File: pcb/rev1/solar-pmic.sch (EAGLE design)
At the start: 82 parts, among them IC2 MCP6002, IC3 MCP6002, IC4 LM3671MF-ADJ, IC5 TS520525, IC6 STM32F030X4, Q1 BSS123

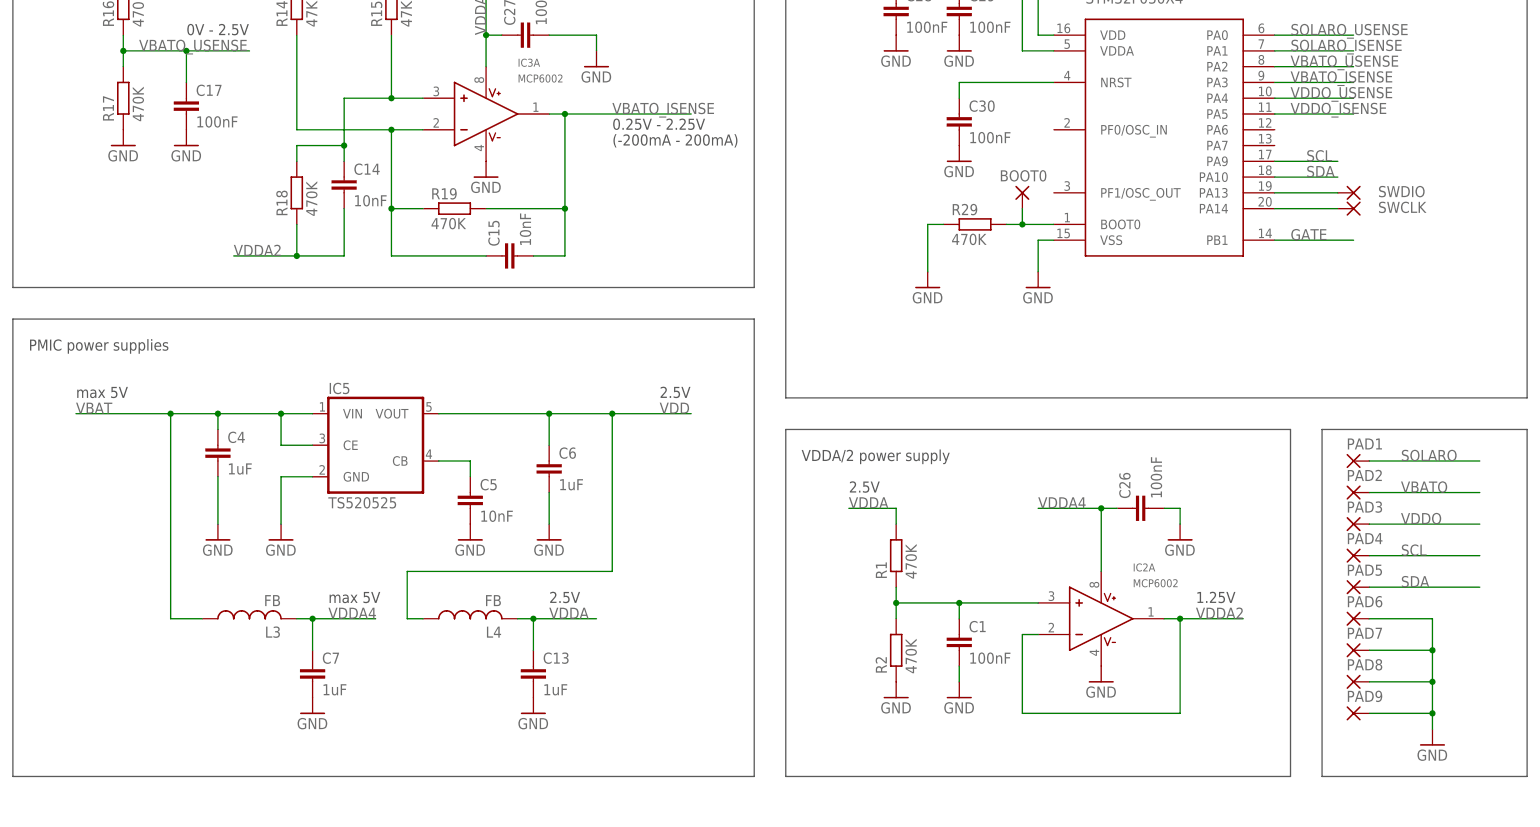
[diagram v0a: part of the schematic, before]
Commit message: Minor schematic fixes + final routing + annotation.
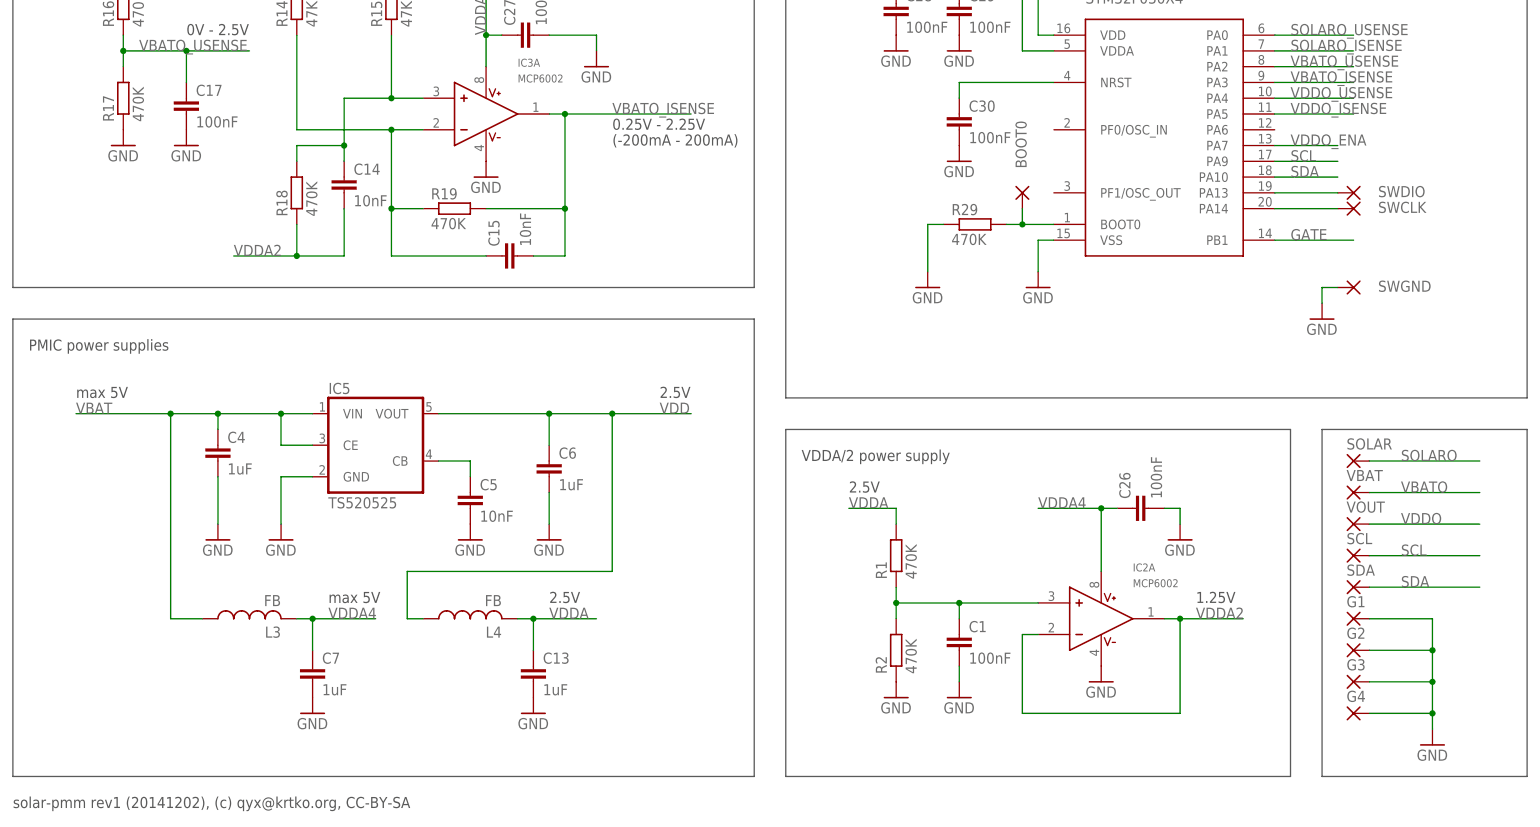
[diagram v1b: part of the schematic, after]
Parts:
- added SWGND: (no value), wirepad:SMD2
- BOOT0: device wirepad:2,15/1,0 -> wirepad:SMD2
- renumbered PAD1 to SOLAR, PAD2 to VBAT, PAD3 to VOUT, PAD4 to SCL, PAD5 to SDA, PAD6 to G1, PAD7 to G2, PAD8 to G3, PAD9 to G4
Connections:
- net GND: now also SWGND.P
- net VDDO_ENA: now also IC6.PA7
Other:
- note added: "solar-pmm rev1 (20141202), (c) qyx@krtko.org, CC-BY-SA"
